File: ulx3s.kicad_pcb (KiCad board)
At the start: 4 copper layers, 94 x 50.8 mm, 113 parts, among them J1 CONN_02X20, J2 CONN_02X20, J3 WIFI_OFF, Q1 BC857, Q2 2N7002, SW1 DIPSW, U1 LFE5U-25F-6BG381C, U10 S25FL164K0XMFI011, U11 PCA9306DCTR, U2 ESP-32S, U3 AP3429A, U4 AP3429A, U5 AP3429A, U6 FT231XS, U7 PCF8523, U9 MT48LC16M16A2TG, Y1 FNETHE025, Y2 32768Hz

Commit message: yellow layer cleanup - removing part of trace leading nowhere
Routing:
- net J2_31-: track 51.7 -> 50.7 mm
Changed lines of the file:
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@@
     (thickness 1.6)
     (drawings 6)
-    (tracks 3961)
+    (tracks 3958)
     (zones 0)
     (modules 145)
@@
   (via (at 145.295462 73.599855) (size 0.4) (drill 0.2) (layers F.Cu B.Cu) (net 172))
   (via (at 141.384492 78.199263) (size 0.4) (drill 0.2) (layers F.Cu B.Cu) (net 172))
-  (segment (start 141.584491 78.399262) (end 141.384492 78.199263) (width 0.19) (layer In1.Cu) (net 172))
-  (segment (start 142.00441 78.819181) (end 141.584491 78.399262) (width 0.19) (layer In1.Cu) (net 172))
-  (segment (start 142.00441 78.9) (end 142.00441 78.819181) (width 0.19) (layer In1.Cu) (net 172))
   (segment (start 141.584491 78.399262) (end 141.384492 78.199263) (width 0.19) (layer B.Cu) (net 172))
   (segment (start 141.65799 78.472761) (end 141.584491 78.399262) (width 0.19) (layer B.Cu) (net 172))

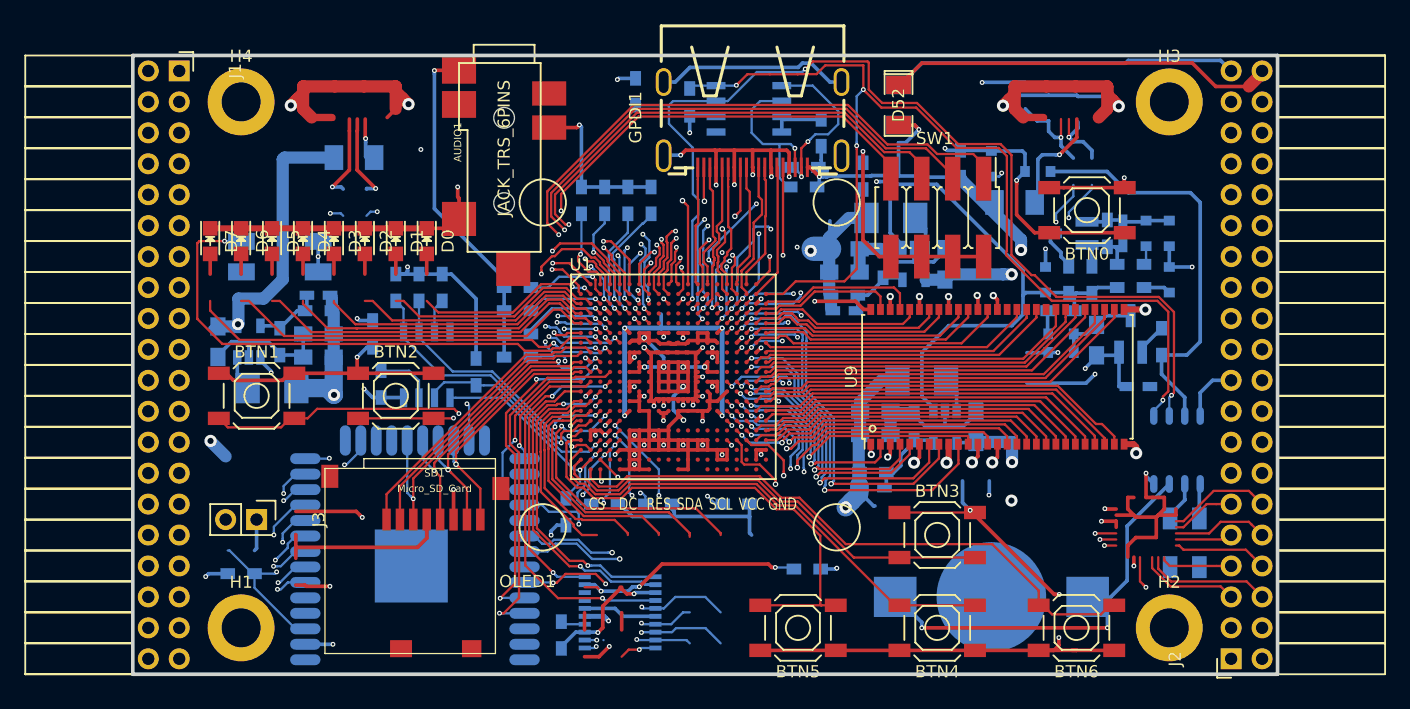
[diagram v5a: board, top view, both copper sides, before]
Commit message: 433 MHz onboard antenna (need to uncover copper infill layers)
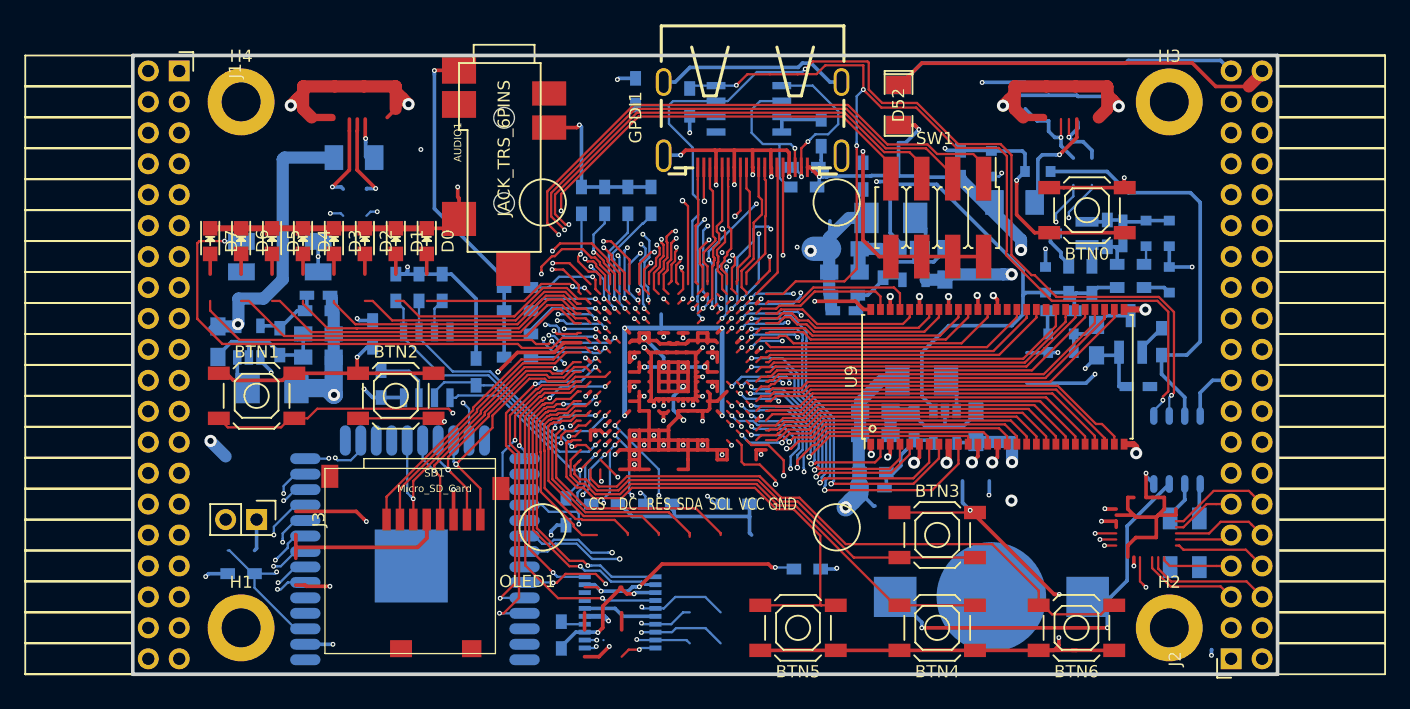
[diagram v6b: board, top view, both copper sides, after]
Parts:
- removed U1: LFE5U-25F-6BG381C, lfe5bg381:BGA-381_pitch0.8mm_dia0.4mm
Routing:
- net /usb/ANT_433MHz: track 0.00 -> 115.4 mm, vias 0 -> 3
- net BTN_PWRn: track 40.8 -> 42.6 mm
- net J1_27-: track 44.0 -> 44.8 mm
- net J1_35+: track 51.3 -> 52.1 mm
- net J1_35-: track 48.6 -> 49.4 mm
- net LED0: track 15.1 -> 14.4 mm
- net J1_33+: track 50.0 -> 50.7 mm
- net WIFI_EN: track 45.7 -> 46.4 mm
- net J1_23-: track 45.4 -> 46.0 mm
- net WIFI_GPIO15: track 14.5 -> 15.1 mm
- net J1_33-: track 46.8 -> 47.3 mm

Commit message: routing 5V using shorter path between 2 USB connectors
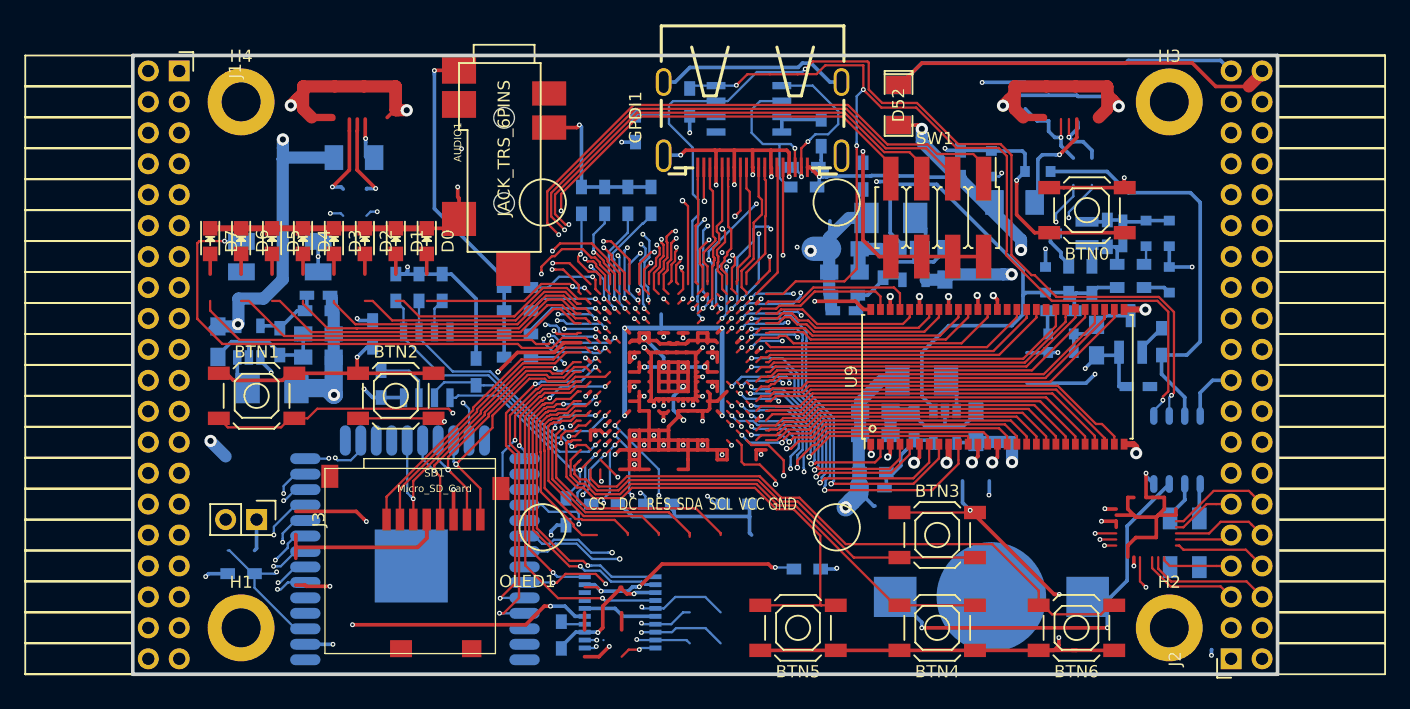
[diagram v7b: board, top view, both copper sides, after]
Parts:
- moved R23 3.03 mm to (135.4, 67.4), turned to 90 degrees
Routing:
- net +5V: track 203.1 -> 214.1 mm, vias 9 -> 10
- net +3V3: track 316.2 -> 310.7 mm
- net /power/PWREN: track 113.0 -> 111.1 mm
- net GND: track 334.9 -> 335.9 mm

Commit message: reducing default solder mask clearance to 0.05 mm it will help preventing shortcuts coming from solder overflow
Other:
- rule pad_to_mask_clearance: 0.2 -> 0.05
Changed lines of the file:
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@@
     (links 672)
     (no_connects 0)
-    (area 71.010001 43.48 197.572001 118.732339)
+    (area 93.949999 61.269999 188.230001 112.370001)
     (thickness 1.6)
     (drawings 6)
@@
     (pad_size 0.5 0.5)
     (pad_drill 0)
-    (pad_to_mask_clearance 0.2)
+    (pad_to_mask_clearance 0.05)
     (aux_axis_origin 82.67 62.69)
     (grid_origin 86.48 79.2)
